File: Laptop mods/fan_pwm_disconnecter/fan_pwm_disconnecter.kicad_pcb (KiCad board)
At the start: 2 copper layers, 26.2 x 8.2 mm, 14 parts, among them J1 IN, J2 OUT, J3 EN, U1 74AHC1G125

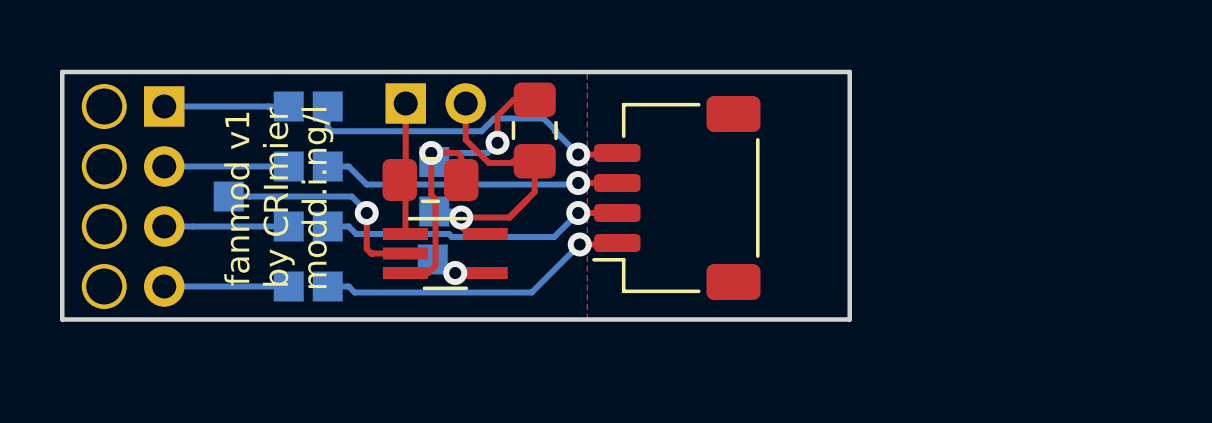
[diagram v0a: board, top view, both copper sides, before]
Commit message: Updated version of the fan_pwm_disconnecter board, this is what I'll be ordering
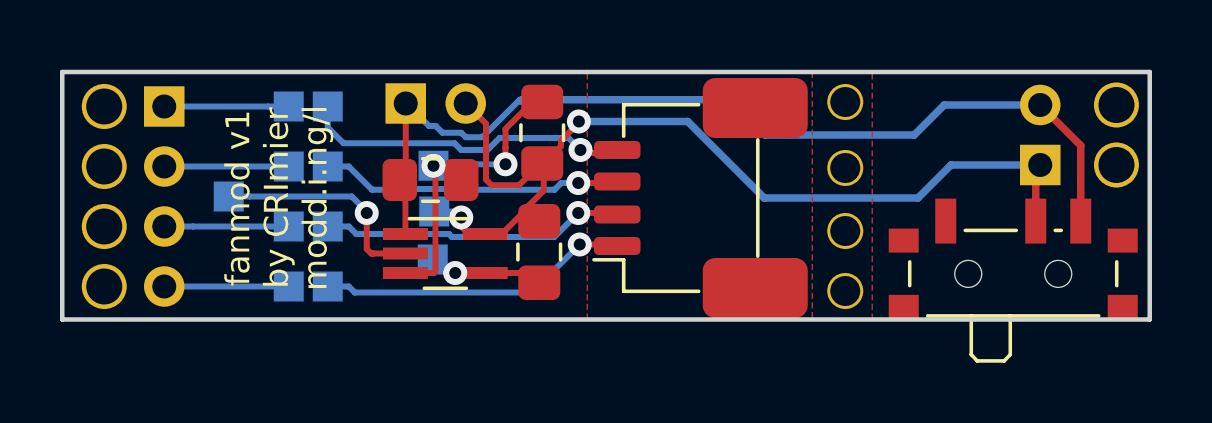
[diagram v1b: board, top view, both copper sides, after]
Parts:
- added H1: MountingHole, fan_pwm_disconnecter:MountingHole_2mm, F.Cu at (156.6, 84.5)
- added H2: MountingHole, fan_pwm_disconnecter:MountingHole_2mm, F.Cu at (156.6, 90.8)
- added H3: MountingHole, fan_pwm_disconnecter:MountingHole_2mm, F.Cu at (156.6, 86.7)
- added H4: MountingHole, fan_pwm_disconnecter:MountingHole_2mm, F.Cu at (156.6, 88.8)
- added J4: SW, Connector_PinHeader_2.00mm:PinHeader_1x04_P2.00mm_Vertical, F.Cu at (163.1, 86.6)
- added R2: 10K, Resistor_SMD:R_0805_2012Metric_Pad1.15x1.40mm_HandSolder, F.Cu at (146.4, 89.5)
- added SW1: SW_SPST, Button_Switch_SMD:SW_SPDT_PCM12, F.Cu at (162.2, 89.9)
- moved C1 0.26 mm to (146.5, 85.5)
- moved TP2 0.13 mm to (142.9, 86.6)
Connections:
- net SHD renamed SHD1
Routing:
- net PWM_DIS: track 4.51 -> 32.2 mm
- net VCC: track 11.3 -> 31.7 mm, vias 1 -> 2
- net PWM_OUT: track 1.94 -> 3.87 mm
- net GND: track 12.4 -> 11.6 mm
- added copper zone on F.Cu, net SHD2
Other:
- board size 26.2 x 8.2 mm -> 36.2 x 8.2 mm
